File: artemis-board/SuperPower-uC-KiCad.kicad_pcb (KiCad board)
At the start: 4 copper layers, 45.1 x 45.1 mm, 81 parts, among them J1 Battery connector, J10 External NTC, J2 Thermistor, J3 USB_B_Micro, J4 Solar in, J7 DNP, J8 regulator board, Q1 2N7002, Q2 2N7002, Q5 AO3401A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

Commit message: applied changes to board
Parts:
- removed R5: 1k, Resistor_SMD:R_0603_1608Metric_Pad1.05x0.95mm_HandSolder
- added C26: 0.1µF, Capacitor_SMD:C_0603_1608Metric_Pad1.05x0.95mm_HandSolder, F.Cu at (151.8, 95.1)
- added Q10: AO3401A, Package_TO_SOT_SMD:SOT-23_Handsoldering, F.Cu at (152.9, 90.9)
- added Q3: 2N7002, Package_TO_SOT_SMD:SOT-23, F.Cu at (159.9, 100.5)
- added R19: 10k, Resistor_SMD:R_0603_1608Metric_Pad1.05x0.95mm_HandSolder, F.Cu at (151.8, 93.5)
- added R20: 10k, Resistor_SMD:R_0603_1608Metric_Pad1.05x0.95mm_HandSolder, F.Cu at (155.3, 93.5)
- added R23: 1M, Resistor_SMD:R_0603_1608Metric_Pad1.05x0.95mm_HandSolder, F.Cu at (156.4, 90.8)
- added R8: 1M, Resistor_SMD:R_0603_1608Metric_Pad1.05x0.95mm_HandSolder, F.Cu at (158.9, 96.9)
- added R9: 1M, Resistor_SMD:R_0603_1608Metric_Pad1.05x0.95mm_HandSolder, F.Cu at (163.3, 101.5)
- R17: value 22k -> 24k
- R18: renamed from R15; value 22k -> 24k
- R22: value 1k -> 2.4k
- moved R3 5.04 mm to (144.2, 93.4)
- moved C2 5.04 mm to (144.2, 90.2)
- moved J2 5.04 mm to (144.2, 91.7)
- moved R2 5.04 mm to (144.2, 95.0)
- moved U3 5.04 mm to (147.8, 93.1)
- moved C9 1.72 mm to (151.8, 99.4)
- moved U8 1.72 mm to (155.3, 99.3)
- moved C8 1.72 mm to (150.1, 99.4)
- moved U7 1.65 mm to (147.2, 103.9)
- moved Y2 1.65 mm to (142.2, 103.2)
- moved R6 1.09 mm to (160.5, 96.9)
- moved R22 0.45 mm to (167.3, 100.4), turned to 0 degrees
- renumbered R19 to R15
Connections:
- net Net-(Q1-Pad1) renamed /RTC and Cut-Off Module/~INT
- J8 pad 13: Net-(J8-Pad13) -> /RTC and Cut-Off Module/Vmeasure
- R22 pad 2: Net-(R22-Pad2) -> GND
- U9 pad 7: /Charging Module/CHARGE-DISABLE -> /RTC and Cut-Off Module/~CH_DIS
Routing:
- net /RTC and Cut-Off Module/Vmeasure: track 0.00 -> 75.7 mm, vias 0 -> 4
- net Net-(Q10-Pad1): track 0.00 -> 15.2 mm, vias 0 -> 2
- net /RTC and Cut-Off Module/~INT: track 7.11 -> 16.9 mm
- net /SCL: track 38.1 -> 43.5 mm
- net /VBUS: track 70.2 -> 75.2 mm
- net /RTC and Cut-Off Module/~CH_DIS: track 0.00 -> 4.94 mm
- net GND: track 66.6 -> 70.9 mm, vias 46 -> 51
- net /SDA: track 38.7 -> 42.9 mm
- net Net-(Q10-Pad3): track 0.00 -> 2.80 mm
- net Net-(J10-Pad2): track 13.7 -> 11.2 mm
- net /Charging Module/CHARGE-DISABLE: track 7.93 -> 6.23 mm
- net Net-(R22-Pad2): track 1.65 -> 0.00 mm
- net /Battery Module/VBAT: track 4.77 -> 3.54 mm
- net Net-(U7-Pad2): track 3.48 -> 2.75 mm

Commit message: updated revision number
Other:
- board text added: "v1.1 (2021-05)"
- board text removed: "v1.00 (2021-02)"
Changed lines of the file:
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@@
-(kicad_pcb (version 20171130) (host pcbnew "(5.1.8)-1")
+(kicad_pcb (version 20171130) (host pcbnew "(5.1.9)-1")
   (general
     (thickness 1.6)
@@
     (34 B.Paste user hide)
     (35 F.Paste user hide)
-    (36 B.SilkS user hide)
+    (36 B.SilkS user)
     (37 F.SilkS user)
     (38 B.Mask user)
@@
       (effects (font (size 1 1) (thickness 0.15)))
     )
-    (fp_text user %R (at 0 0) (layer F.Fab)
-      (effects (font (size 0.4 0.4) (thickness 0.06)))
-    )
     (fp_line (start -0.8 0.4) (end -0.8 -0.4) (layer F.Fab) (width 0.1))
     (fp_line (start -0.8 -0.4) (end 0.8 -0.4) (layer F.Fab) (width 0.1))
@@
     (fp_line (start 1.65 -0.73) (end 1.65 0.73) (layer F.CrtYd) (width 0.05))
     (fp_line (start 1.65 0.73) (end -1.65 0.73) (layer F.CrtYd) (width 0.05))
+    (fp_text user %R (at 0 0) (layer F.Fab)
+      (effects (font (size 0.4 0.4) (thickness 0.06)))
+    )
     (pad 2 smd roundrect (at 0.875 0) (size 1.05 0.95) (layers F.Cu F.Paste F.Mask) (roundrect_rratio 0.25)
       (net 2 GND))
@@
       (effects (font (size 1 1) (thickness 0.15)))
     )
-    (fp_text user %R (at 0 0 90) (layer F.Fab)
-      (effects (font (size 0.4 0.4) (thickness 0.06)))
-    )
     (fp_line (start -0.8 0.4) (end -0.8 -0.4) (layer F.Fab) (width 0.1))
     (fp_line (start -0.8 -0.4) (end 0.8 -0.4) (layer F.Fab) (width 0.1))
@@
     (fp_line (start 1.65 -0.73) (end 1.65 0.73) (layer F.CrtYd) (width 0.05))
     (fp_line (start 1.65 0.73) (end -1.65 0.73) (layer F.CrtYd) (width 0.05))
+    (fp_text user %R (at 0 0 90) (layer F.Fab)
+      (effects (font (size 0.4 0.4) (thickness 0.06)))
+    )
     (pad 2 smd roundrect (at 0.875 0 90) (size 1.05 0.95) (layers F.Cu F.Paste F.Mask) (roundrect_rratio 0.25)
       (net 7 "/Battery Module/VBAT"))
@@
       (effects (font (size 1 1) (thickness 0.15)))
     )
-    (fp_text user %R (at 0 0) (layer F.Fab)
-      (effects (font (size 0.4 0.4) (thickness 0.06)))
-    )
     (fp_line (start -0.8 0.4) (end -0.8 -0.4) (layer F.Fab) (width 0.1))
     (fp_line (start -0.8 -0.4) (end 0.8 -0.4) (layer F.Fab) (width 0.1))
@@
     (fp_line (start 1.65 -0.73) (end 1.65 0.73) (layer F.CrtYd) (width 0.05))
     (fp_line (start 1.65 0.73) (end -1.65 0.73) (layer F.CrtYd) (width 0.05))
+    (fp_text user %R (at 0 0) (layer F.Fab)
+      (effects (font (size 0.4 0.4) (thickness 0.06)))
+    )
     (pad 2 smd roundrect (at 0.875 0) (size 1.05 0.95) (layers F.Cu F.Paste F.Mask) (roundrect_rratio 0.25)
       (net 2 GND))
@@
       (effects (font (size 1 1) (thickness 0.15)))
     )
-    (fp_text user %R (at 0 0) (layer F.Fab)
-      (effects (font (size 0.4 0.4) (thickness 0.06)))
-    )
     (fp_line (start -0.8 0.4) (end -0.8 -0.4) (layer F.Fab) (width 0.1))
     (fp_line (start -0.8 -0.4) (end 0.8 -0.4) (layer F.Fab) (width 0.1))
@@
     (fp_line (start 1.65 -0.73) (end 1.65 0.73) (layer F.CrtYd) (width 0.05))
     (fp_line (start 1.65 0.73) (end -1.65 0.73) (layer F.CrtYd) (width 0.05))
+    (fp_text user %R (at 0 0) (layer F.Fab)
+      (effects (font (size 0.4 0.4) (thickness 0.06)))
+    )
     (pad 2 smd roundrect (at 0.875 0) (size 1.05 0.95) (layers F.Cu F.Paste F.Mask) (roundrect_rratio 0.25)
       (net 55 "/RTC and Cut-Off Module/Vmeasure"))
@@
       (effects (font (size 1 1) (thickness 0.15)))
     )
-    (fp_text user %R (at 0 0) (layer F.Fab)
-      (effects (font (size 0.4 0.4) (thickness 0.06)))
-    )
     (fp_line (start -0.8 0.4) (end -0.8 -0.4) (layer F.Fab) (width 0.1))
     (fp_line (start -0.8 -0.4) (end 0.8 -0.4) (layer F.Fab) (width 0.1))
@@
     (fp_line (start 1.65 -0.73) (end 1.65 0.73) (layer F.CrtYd) (width 0.05))
     (fp_line (start 1.65 0.73) (end -1.65 0.73) (layer F.CrtYd) (width 0.05))
+    (fp_text user %R (at 0 0) (layer F.Fab)
+      (effects (font (size 0.4 0.4) (thickness 0.06)))
+    )
     (pad 2 smd roundrect (at 0.875 0 180) (size 1.05 0.95) (layers F.Cu F.Paste F.Mask) (roundrect_rratio 0.25)
       (net 57 "/RTC and Cut-Off Module/~CH_DIS"))
@@
       (effects (font (size 1 1) (thickness 0.15)))
     )
-    (fp_text user %R (at 0 0 90) (layer F.Fab)
-      (effects (font (size 0.4 0.4) (thickness 0.06)))
-    )
     (fp_line (start -0.8 0.4) (end -0.8 -0.4) (layer F.Fab) (width 0.1))
     (fp_line (start -0.8 -0.4) (end 0.8 -0.4) (layer F.Fab) (width 0.1))
@@
     (fp_line (start 1.65 -0.73) (end 1.65 0.73) (layer F.CrtYd) (width 0.05))
     (fp_line (start 1.65 0.73) (end -1.65 0.73) (layer F.CrtYd) (width 0.05))
+    (fp_text user %R (at 0 0 90) (layer F.Fab)
+      (effects (font (size 0.4 0.4) (thickness 0.06)))
+    )
     (pad 2 smd roundrect (at 0.875 0 270) (size 1.05 0.95) (layers F.Cu F.Paste F.Mask) (roundrect_rratio 0.25)
       (net 56 "/RTC and Cut-Off Module/~INT"))
@@
       (effects (font (size 1 1) (thickness 0.15)))
     )
-    (fp_text user %R (at 0 0 90) (layer F.Fab)
-      (effects (font (size 0.5 0.5) (thickness 0.075)))
-    )
     (fp_line (start 0.76 1.58) (end 0.76 0.65) (layer F.SilkS) (width 0.12))
     (fp_line (start 0.76 -1.58) (end 0.76 -0.65) (layer F.SilkS) (width 0.12))
@@
     (fp_line (start -0.7 1.52) (end 0.7 1.52) (layer F.Fab) (width 0.1))
     (fp_line (start 0.76 1.58) (end -0.7 1.58) (layer F.SilkS) (width 0.12))
+    (fp_text user %R (at 0 0 90) (layer F.Fab)
+      (effects (font (size 0.5 0.5) (thickness 0.075)))
+    )
     (pad 3 smd rect (at 1.5 0 180) (size 1.9 0.8) (layers F.Cu F.Paste F.Mask)
       (net 58 "Net-(Q10-Pad3)"))
@@
       (effects (font (size 1 1) (thickness 0.15)))
     )
-    (fp_text user %R (at 0 0 90) (layer F.Fab)
-      (effects (font (size 0.5 0.5) (thickness 0.075)))
-    )
     (fp_line (start -0.7 -0.95) (end -0.7 1.5) (layer F.Fab) (width 0.1))
     (fp_line (start -0.15 -1.52) (end 0.7 -1.52) (layer F.Fab) (width 0.1))
@@
     (fp_line (start 0.76 -1.58) (end -1.4 -1.58) (layer F.SilkS) (width 0.12))
     (fp_line (start 0.76 1.58) (end -0.7 1.58) (layer F.SilkS) (width 0.12))
+    (fp_text user %R (at 0 0 90) (layer F.Fab)
+      (effects (font (size 0.5 0.5) (thickness 0.075)))
+    )
     (pad 3 smd rect (at 1 0 180) (size 0.9 0.8) (layers F.Cu F.Paste F.Mask)
       (net 48 "/Charging Module/CHARGE-DISABLE"))
@@
       (effects (font (size 1 1) (thickness 0.15)))
     )
-    (fp_text user %R (at 0 0) (layer F.Fab)
-      (effects (font (size 0.4 0.4) (thickness 0.06)))
-    )
     (fp_line (start -0.8 0.4) (end -0.8 -0.4) (layer F.Fab) (width 0.1))
     (fp_line (start -0.8 -0.4) (end 0.8 -0.4) (layer F.Fab) (width 0.1))
@@
     (fp_line (start 1.65 -0.73) (end 1.65 0.73) (layer F.CrtYd) (width 0.05))
     (fp_line (start 1.65 0.73) (end -1.65 0.73) (layer F.CrtYd) (width 0.05))
+    (fp_text user %R (at 0 0) (layer F.Fab)
+      (effects (font (size 0.4 0.4) (thickness 0.06)))
+    )
     (pad 2 smd roundrect (at 0.875 0) (size 1.05 0.95) (layers F.Cu F.Paste F.Mask) (roundrect_rratio 0.25)
       (net 55 "/RTC and Cut-Off Module/Vmeasure"))
@@
     (effects (font (size 0.8 0.8) (thickness 0.15)) (justify mirror))
   )
-  (gr_text "v1.00 (2021-02)" (at 148.91512 105.69956) (layer B.SilkS)
+  (gr_text "v1.1 (2021-05)" (at 148.91512 105.69956) (layer B.SilkS)
     (effects (font (size 0.8 0.8) (thickness 0.15)) (justify mirror))
   )
@@
   (segment (start 168.1581 101.318) (end 168.1861 101.346) (width 0.25) (layer F.Cu) (net 2))
   (segment (start 168.1581 100.3935) (end 168.1581 101.318) (width 0.25) (layer F.Cu) (net 2))
-  (segment (start 166.2176 105.1458) (end 166.2176 104.393994) (width 0.25) (layer F.Cu) (net 56))
-  (via (at 166.2176 104.393994) (size 0.6) (drill 0.3) (layers F.Cu B.Cu) (net 56))
   (segment (start 145.4531 93.3577) (end 145.0975 93.3577) (width 0.25) (layer F.Cu) (net 4))
   (segment (start 146.8149 94.7195) (end 145.4531 93.3577) (width 0.25) (layer F.Cu) (net 4))
@@
   (segment (start 162.9068 96.1644) (end 161.67099 96.1644) (width 0.25) (layer F.Cu) (net 22))
   (segment (start 161.67099 96.1644) (end 161.58209 96.0755) (width 0.25) (layer F.Cu) (net 22))
-  (segment (start 154.9146 118.011) (end 156.4386 118.011) (width 0.25) (layer F.Cu) (net 60))
-  (segment (start 154.9146 117.856) (end 154.9146 118.011) (width 0.25) (layer F.Cu) (net 60))
-  (segment (start 153.3856 116.327) (end 154.9146 117.856) (width 0.25) (layer F.Cu) (net 60))
-  (segment (start 153.129 116.327) (end 153.3856 116.327) (width 0.25) (layer F.Cu) (net 60))
   (segment (start 155.829 113.03) (end 156.083 112.776) (width 0.25) (layer F.Cu) (net 23))
   (segment (start 155.829 114.427) (end 155.829 113.03) (width 0.25) (layer F.Cu) (net 23))
@@
   (segment (start 152.7556 88.467484) (end 153.009594 88.21349) (width 0.25) (layer B.Cu) (net 55))
   (segment (start 152.7556 92.1385) (end 152.7556 88.467484) (width 0.25) (layer B.Cu) (net 55))
+  (segment (start 166.2176 105.1458) (end 166.2176 104.393994) (width 0.25) (layer F.Cu) (net 56))
+  (via (at 166.2176 104.393994) (size 0.6) (drill 0.3) (layers F.Cu B.Cu) (net 56))
   (via (at 161.5186 105.41) (size 0.6) (drill 0.3) (layers F.Cu B.Cu) (net 56))
   (segment (start 162.7378 105.4458) (end 161.5544 105.4458) (width 0.25) (layer F.Cu) (net 56))
@@
   (segment (start 154.4066 91.816) (end 155.30659 92.71599) (width 0.25) (layer F.Cu) (net 59))
   (segment (start 155.30659 100.30219) (end 156.1846 101.1802) (width 0.25) (layer F.Cu) (net 59))
+  (segment (start 154.9146 118.011) (end 156.4386 118.011) (width 0.25) (layer F.Cu) (net 60))
+  (segment (start 154.9146 117.856) (end 154.9146 118.011) (width 0.25) (layer F.Cu) (net 60))
+  (segment (start 153.3856 116.327) (end 154.9146 117.856) (width 0.25) (layer F.Cu) (net 60))
+  (segment (start 153.129 116.327) (end 153.3856 116.327) (width 0.25) (layer F.Cu) (net 60))
   (zone (net 7) (net_name "/Battery Module/VBAT") (layer F.Cu) (hatch edge 0.508)
     (connect_pads (clearance 0.21))

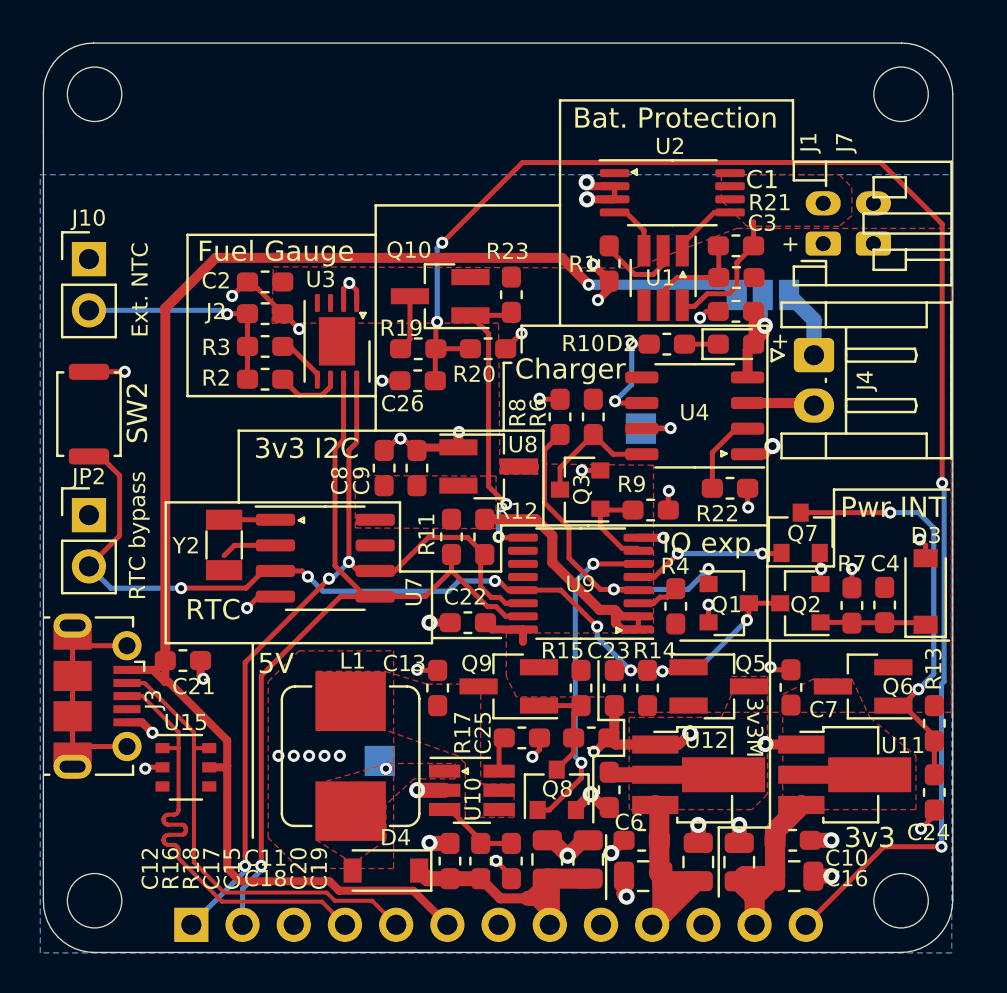
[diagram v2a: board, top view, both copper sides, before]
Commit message: changed the layout a bit and removed TP on boost converter
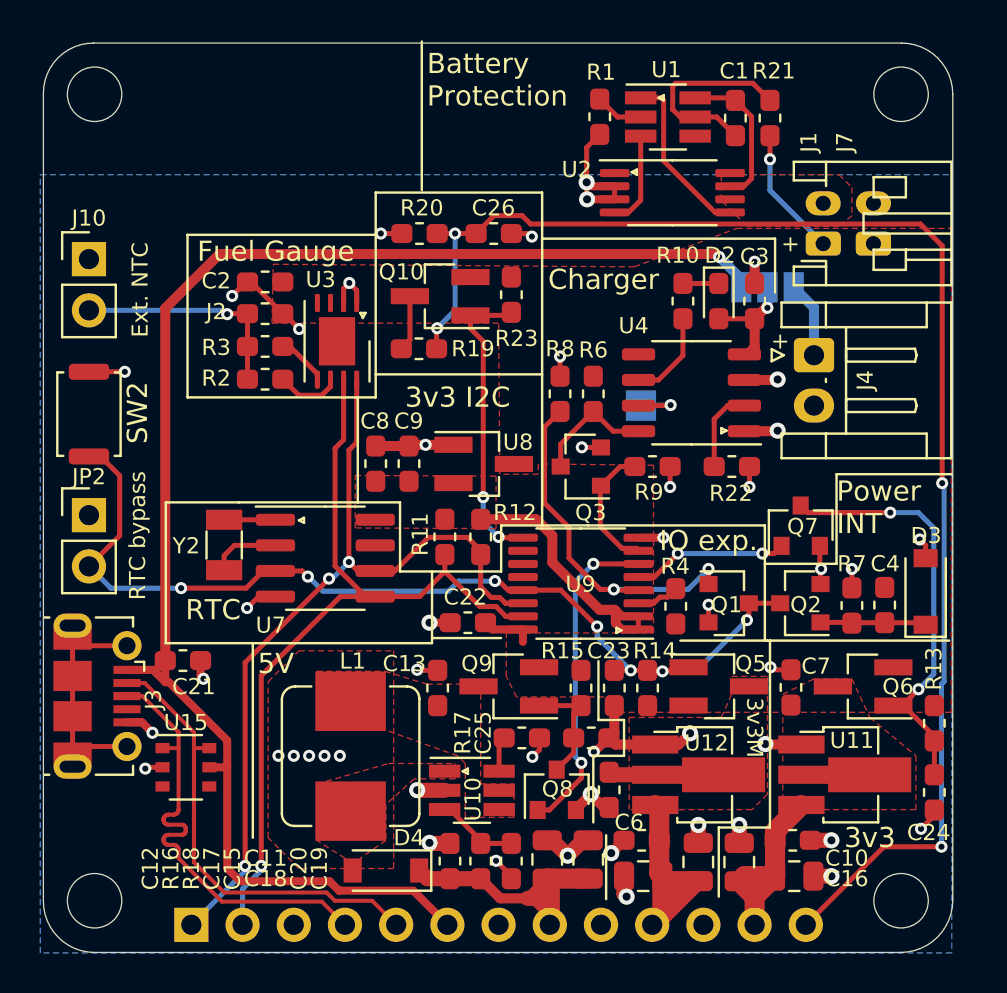
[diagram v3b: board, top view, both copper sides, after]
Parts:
- removed TP5: TestPoint, TestPoint:TestPoint_Pad_1.5x1.5mm
- moved C26 8.22 mm to (155.6, 87.8), turned to 180 degrees
- moved R21 8.09 mm to (169.3, 82.0), turned to 90 degrees
- moved U1 7.99 mm to (164.2, 82.0), turned to 0 degrees
- moved R1 7.29 mm to (160.8, 82.0)
- moved R20 6.65 mm to (151.9, 87.8), turned to 180 degrees
- moved C1 6.34 mm to (167.6, 82.0), turned to 90 degrees
- moved D2 2.30 mm to (166.7, 91.1), turned to 270 degrees
- moved R10 2.28 mm to (164.9, 91.1), turned to 270 degrees
- moved R9 2.16 mm to (163.4, 99.3)
- moved U4 1.15 mm to (165.4, 95.7)
- moved Q3 1.14 mm to (159.9, 99.3)
- moved R6 1.14 mm to (160.5, 95.7)
- moved R8 1.14 mm to (158.9, 95.7)
- moved TP4 1.14 mm to (162.9, 96.3)
- moved R22 1.08 mm to (167.4, 99.3)
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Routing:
- net /Battery Module/VBAT: track 3.54 -> 9.99 mm, vias 0 -> 1
- net /RTC and Cut-Off Module/Vmeasure: track 75.7 -> 70.4 mm
- net Net-(U1-Pad1): track 3.40 -> 8.56 mm
- net Net-(C1-Pad1): track 5.37 -> 10.0 mm
- net Net-(U1-Pad3): track 2.90 -> 4.72 mm
- net Net-(R1-Pad1): track 4.18 -> 2.40 mm
- net /RTC and Cut-Off Module/~CH_DIS: track 4.94 -> 6.60 mm
- net /RTC and Cut-Off Module/~INT: track 16.9 -> 18.1 mm
- net /Charging Module/STDBY: track 5.44 -> 4.37 mm, vias 2 -> 0
- net GND: track 70.9 -> 69.9 mm, vias 51 -> 49
- net /Charger I/O/VCHARGE: track 7.53 -> 6.69 mm
- net /Battery Module/BAT-: track 6.66 -> 7.48 mm
- net Net-(U7-Pad2): track 2.75 -> 3.48 mm
- net Net-(D4-Pad2): vias 1 -> 0
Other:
- board text added: "Battery Protection"
- board text added: "NC"
- board text added: "Power INT"
- board text added: "VBat/2"
- board text removed: "3v3 EN"
- board text removed: "5v EN"
- board text removed: "Bat. Protection"
- board text removed: "Pwr INT"
- board text removed: "~SMBALERT"

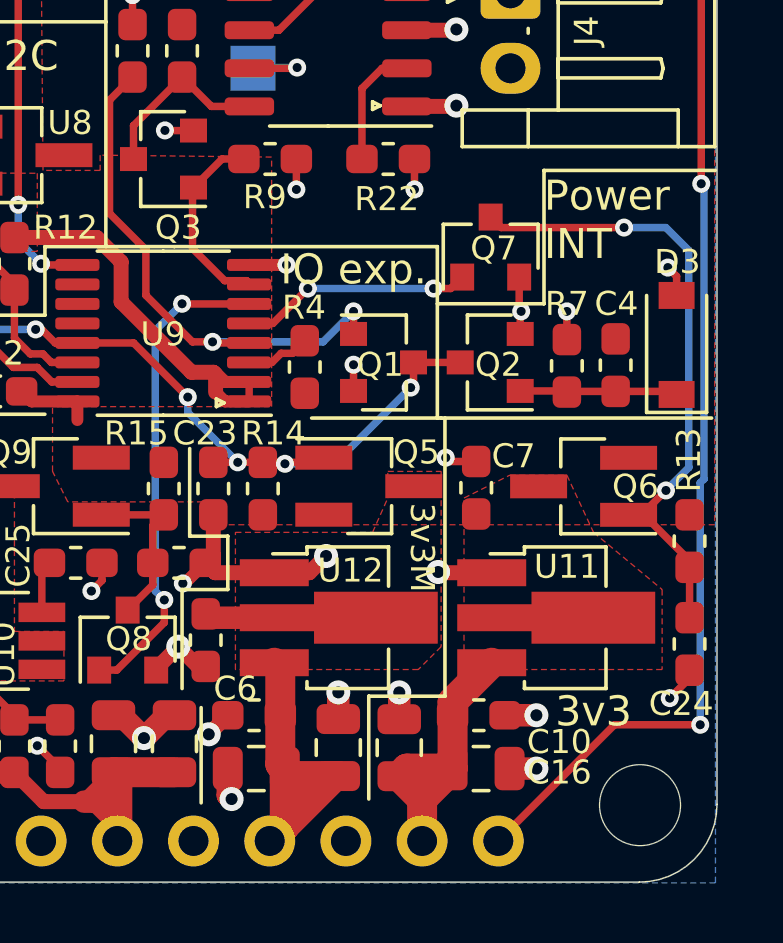
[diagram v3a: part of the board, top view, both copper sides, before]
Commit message: moved Vbat/2 line to other pin on the header
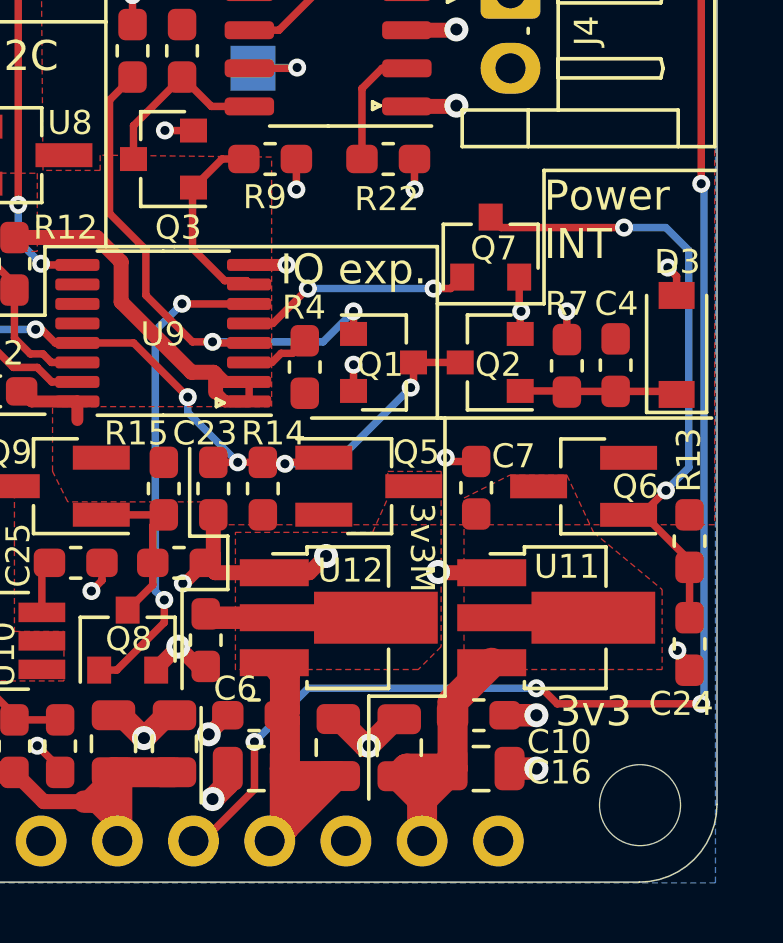
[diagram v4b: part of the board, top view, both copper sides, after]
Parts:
- L1: value 3.3u -> 6.8µH
- R17: value 24k -> 39k
- U1: value AP9101CK6-ADTRG1 -> FS312F-G
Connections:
- J8 pad 13: /RTC and Cut-Off Module/Vmeasure -> Net-(J8-Pad13)
- J8 pad 9: Net-(J8-Pad9) -> /RTC and Cut-Off Module/Vmeasure
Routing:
- net /RTC and Cut-Off Module/Vmeasure: track 70.4 -> 81.8 mm, vias 4 -> 6
- net GND: track 69.9 -> 70.7 mm, vias 49 -> 48
